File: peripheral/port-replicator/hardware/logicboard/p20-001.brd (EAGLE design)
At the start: 72 x 72 mm, 25 parts, among them IC1 74ALS04N, J0 DC9V, J11 AUDIO_JACK_3.5MM_PTH, J12 AUDIO_JACK_3.5MM_PTH, J13 AUDIO_JACK_3.5MM_PTH, J14 AUDIO_JACK_3.5MM_PTH, J21 DIN5, J22 DIN5, J23 DIN5, X0 MKDSN1,5/2-5,08

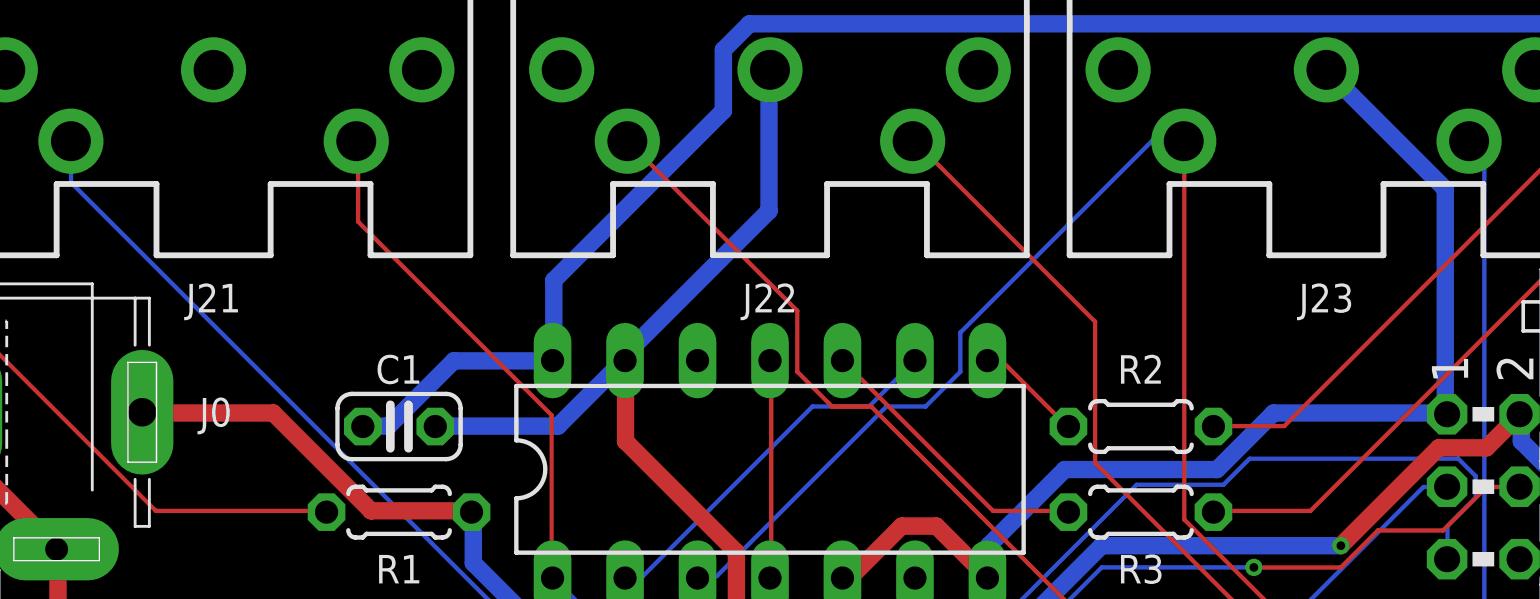
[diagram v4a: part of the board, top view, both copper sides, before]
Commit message: Renumbered parts of Port Replicator.
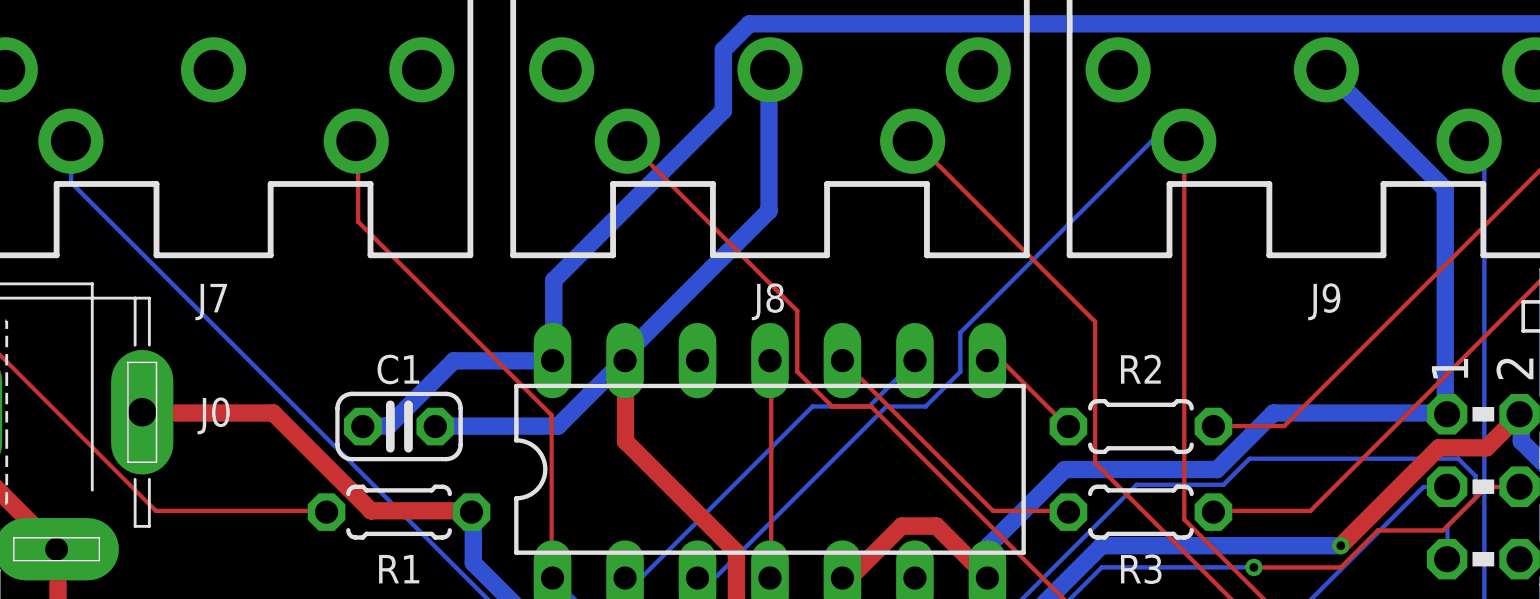
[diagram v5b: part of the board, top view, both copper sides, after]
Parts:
- renumbered J21 to J7, J22 to J8, J23 to J9
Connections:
- net MRX+: now also SV2.7; no longer SV2.6
- net MRXDTCT: now also SV2.6; no longer SV2.7
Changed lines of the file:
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@@
 <attribute name="VALUE" x="-0.43" y="27.9746" size="1.778" layer="27" ratio="10" rot="R90"/>
 </element>
-<element name="J21" library="SparkFun-Connectors" library_urn="urn:adsk.eagle:library:513" package="DIN5-RA-PTH" package3d_urn="urn:adsk.eagle:package:38294/1" value="DIN5" x="16.5" y="72" smashed="yes" rot="R180">
+<element name="J7" library="SparkFun-Connectors" library_urn="urn:adsk.eagle:library:513" package="DIN5-RA-PTH" package3d_urn="urn:adsk.eagle:package:38294/1" value="DIN5" x="16.5" y="72" smashed="yes" rot="R180">
 <attribute name="NAME" x="16.5" y="52" size="1" layer="25" ratio="20" align="top-center"/>
 <attribute name="PROD_ID" value="CONN-09481" x="16.5" y="72" size="1.778" layer="27" rot="R180" display="off"/>
 <attribute name="VALUE" x="17.77" y="68.063" size="0.6096" layer="27" font="vector" ratio="20" rot="R180"/>
 </element>
-<element name="J22" library="SparkFun-Connectors" library_urn="urn:adsk.eagle:library:513" package="DIN5-RA-PTH" package3d_urn="urn:adsk.eagle:package:38294/1" value="DIN5" x="36" y="72" smashed="yes" rot="R180">
+<element name="J8" library="SparkFun-Connectors" library_urn="urn:adsk.eagle:library:513" package="DIN5-RA-PTH" package3d_urn="urn:adsk.eagle:package:38294/1" value="DIN5" x="36" y="72" smashed="yes" rot="R180">
 <attribute name="NAME" x="36" y="52" size="1" layer="25" ratio="20" align="top-center"/>
 <attribute name="PROD_ID" value="CONN-09481" x="36" y="72" size="1.778" layer="27" rot="R180" display="off"/>
 <attribute name="VALUE" x="37.27" y="68.063" size="0.6096" layer="27" font="vector" ratio="20" rot="R180"/>
 </element>
-<element name="J23" library="SparkFun-Connectors" library_urn="urn:adsk.eagle:library:513" package="DIN5-RA-PTH" package3d_urn="urn:adsk.eagle:package:38294/1" value="DIN5" x="55.5" y="72" smashed="yes" rot="R180">
+<element name="J9" library="SparkFun-Connectors" library_urn="urn:adsk.eagle:library:513" package="DIN5-RA-PTH" package3d_urn="urn:adsk.eagle:package:38294/1" value="DIN5" x="55.5" y="72" smashed="yes" rot="R180">
 <attribute name="NAME" x="55.5" y="52" size="1" layer="25" ratio="20" align="top-center"/>
 <attribute name="PROD_ID" value="CONN-09481" x="55.5" y="72" size="1.778" layer="27" rot="R180" display="off"/>
@@
 <contactref element="J0" pad="1"/>
 <contactref element="J0" pad="2"/>
-<contactref element="J22" pad="2"/>
-<contactref element="J23" pad="2"/>
+<contactref element="J8" pad="2"/>
+<contactref element="J9" pad="2"/>
 <contactref element="J11" pad="SLEEVE"/>
 <contactref element="J12" pad="SLEEVE"/>
@@
 <wire x1="39.7764" y1="21.336" x2="39.81" y2="21.27" width="0.1524" layer="1"/>
 </signal>
-<signal name="MRX+">
-<contactref element="SV2" pad="6"/>
-</signal>
 <signal name="MRX-">
 <contactref element="SV2" pad="8"/>
 </signal>
 <signal name="MRXDTCT">
-<contactref element="SV2" pad="7"/>
+<contactref element="SV2" pad="6"/>
 </signal>
 <signal name="VCC/2" class="2">
@@
 </signal>
 <signal name="MISND">
-<contactref element="J21" pad="4"/>
+<contactref element="J7" pad="4"/>
 <contactref element="SV2" pad="4"/>
 <wire x1="61.1124" y1="44.8818" x2="62.2554" y2="44.8818" width="0.1524" layer="1"/>
@@
 </signal>
 <signal name="MIRTN">
-<contactref element="J21" pad="5"/>
+<contactref element="J7" pad="5"/>
 <contactref element="IC1" pad="1"/>
 <contactref element="SV2" pad="5"/>
@@
 </signal>
 <signal name="MORTN">
-<contactref element="J23" pad="5"/>
+<contactref element="J9" pad="5"/>
 <contactref element="SV2" pad="15"/>
 <wire x1="59.7408" y1="30.861" x2="59.7408" y2="29.718" width="0.1524" layer="16"/>
@@
 </signal>
 <signal name="MOSND">
-<contactref element="J23" pad="4"/>
+<contactref element="J9" pad="4"/>
 <contactref element="IC1" pad="3"/>
 <contactref element="SV2" pad="14"/>
@@
 <signal name="MTSND">
 <contactref element="SV2" pad="17"/>
-<contactref element="J22" pad="4"/>
+<contactref element="J8" pad="4"/>
 <wire x1="59.6646" y1="27.5844" x2="59.6646" y2="27.1272" width="0.1524" layer="1"/>
 <wire x1="39.5478" y1="47.7012" x2="59.6646" y2="27.5844" width="0.1524" layer="1"/>
@@
 <signal name="MTRTN">
 <contactref element="SV2" pad="18"/>
-<contactref element="J22" pad="5"/>
+<contactref element="J8" pad="5"/>
 <wire x1="62.2554" y1="28.2702" x2="62.2554" y2="27.1272" width="0.1524" layer="1"/>
 <wire x1="60.7314" y1="29.7942" x2="62.2554" y2="28.2702" width="0.1524" layer="1"/>
@@
 <wire x1="38.5572" y1="49.3014" x2="38.54" y2="49.31" width="0.1524" layer="1"/>
 </signal>
+<signal name="MRX+">
+<contactref element="SV2" pad="7"/>
+</signal>
 </signals>

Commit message: Redesign of port rep.
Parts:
- removed JP1: (no value), adafruit:2X04
- added RN1, RN2: (no value), resistor-net:RN-5
- added S2: (no value), switch-dil:DIP04S
- moved S1 2.00 mm to (36.0, 29.5)
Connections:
- new net N$5: RN2.2, S2.8
- new net N$6: RN2.3, S2.7
- new net N$7: RN2.4, S2.6
- new net N$8: RN2.5, S2.5
- net DTCT1: now also J11.TSH, RN1.2, S2.1; no longer JP1.2
- net DTCT2: now also J12.TSH, RN1.3, S2.2; no longer JP1.4
- net DTCT3: now also J13.TSH, RN1.4, S2.3; no longer JP1.6
- net DTCT4: now also J14.TSH, RN1.5, S2.4; no longer JP1.8
- net GND: now also RN1.1; no longer JP1.1, JP1.3, JP1.5, JP1.7
- net VCC/2: now also RN2.1
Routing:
- net DTCT4: track 34.0 -> 88.3 mm
- net DTCT3: track 29.4 -> 60.4 mm
- net GND: track 293.5 -> 267.9 mm
- net N$5: track 0.00 -> 18.8 mm
- net N$6: track 0.00 -> 17.3 mm
- net DTCT1: track 20.1 -> 36.9 mm
- net VCC/2: track 79.2 -> 96.0 mm
- net N$7: track 0.00 -> 14.5 mm
- net MOSND: track 54.8 -> 67.9 mm
- net N$8: track 0.00 -> 13.1 mm
- net V+: track 90.2 -> 102.5 mm, vias 1 -> 0
- net ANLG2R: track 21.4 -> 32.5 mm
- net LED0: track 117.8 -> 125.8 mm
- net DTCT2: track 24.7 -> 32.6 mm
- net MISND: track 61.5 -> 67.6 mm, vias 1 -> 0
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- removed copper zone on layer 1, net GND
- removed copper zone on layer 16, net GND
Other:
- board text added: "Active"
- board text added: "Passive"

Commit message: Renumbered parts of Pineapple II and port rep.
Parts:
- renumbered C1 to C11, IC1 to IC11, R1 to R11
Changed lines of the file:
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@@
 </element>
 <element name="U$1" library="pineapple" package="PINEAPPLE450_SILK" value="PINEAPPLE450_SILK" x="36" y="33.5" smashed="yes" rot="MR0"/>
-<element name="C1" library="resistor" library_urn="urn:adsk.eagle:library:348" package="C025-024X044" package3d_urn="urn:adsk.eagle:package:23630/1" value="10n" x="23" y="47" smashed="yes">
+<element name="C11" library="resistor" library_urn="urn:adsk.eagle:library:348" package="C025-024X044" package3d_urn="urn:adsk.eagle:package:23630/1" value="10n" x="23" y="47" smashed="yes">
 <attribute name="NAME" x="23" y="48.5" size="1" layer="25" ratio="10" align="bottom-center"/>
 <attribute name="VALUE" x="23" y="45" size="0.8128" layer="27" ratio="10" align="bottom-center"/>
@@
 <attribute name="VALUE" x="59.667" y="5.23" size="0.6096" layer="27" font="vector" ratio="20" rot="R90"/>
 </element>
-<element name="IC1" library="74xx-us" library_urn="urn:adsk.eagle:library:88" package="DIL14" package3d_urn="urn:adsk.eagle:package:16407/2" value="74ALS04N" x="36" y="45.5" smashed="yes">
+<element name="IC11" library="74xx-us" library_urn="urn:adsk.eagle:library:88" package="DIL14" package3d_urn="urn:adsk.eagle:package:16407/2" value="74ALS04N" x="36" y="45.5" smashed="yes">
 <attribute name="NAME" x="36" y="40" size="1" layer="25" ratio="10" align="top-center"/>
 <attribute name="POPULARITY" value="10" x="36" y="45.5" size="1.778" layer="27" display="off"/>
 <attribute name="VALUE" x="29.269" y="44.865" size="1.27" layer="27" ratio="10"/>
 </element>
-<element name="R1" library="rcl" library_urn="urn:adsk.eagle:library:334" package="0204/5" package3d_urn="urn:adsk.eagle:package:23488/1" value="" x="23" y="44" smashed="yes">
+<element name="R11" library="rcl" library_urn="urn:adsk.eagle:library:334" package="0204/5" package3d_urn="urn:adsk.eagle:package:23488/1" value="" x="23" y="44" smashed="yes">
 <attribute name="NAME" x="23" y="42.5" size="1" layer="25" ratio="10" align="top-center"/>
 <attribute name="POPULARITY" value="35" x="23" y="44" size="1.778" layer="27" display="off"/>
@@
 <signals>
 <signal name="GND" class="1">
-<contactref element="C1" pad="2"/>
+<contactref element="C11" pad="2"/>
 <contactref element="SV1" pad="1"/>
 <contactref element="SV1" pad="5"/>
@@
 <contactref element="J13" pad="SLEEVE"/>
 <contactref element="J14" pad="SLEEVE"/>
-<contactref element="IC1" pad="13"/>
-<contactref element="IC1" pad="5"/>
+<contactref element="IC11" pad="13"/>
+<contactref element="IC11" pad="5"/>
 <contactref element="LED4" pad="K"/>
-<contactref element="IC1" pad="7"/>
+<contactref element="IC11" pad="7"/>
 <contactref element="X0" pad="1"/>
 <contactref element="S1" pad="1"/>
@@
 </signal>
 <signal name="VCC" class="2">
-<contactref element="C1" pad="1"/>
+<contactref element="C11" pad="1"/>
 <contactref element="LED2" pad="A"/>
 <contactref element="LED3" pad="A"/>
-<contactref element="IC1" pad="14"/>
+<contactref element="IC11" pad="14"/>
 <contactref element="SV2" pad="12"/>
 <wire x1="22.6314" y1="47.0154" x2="21.7932" y2="47.0154" width="0.6096" layer="16"/>
@@
 <signal name="MIRTN">
 <contactref element="J7" pad="5"/>
-<contactref element="IC1" pad="1"/>
+<contactref element="IC11" pad="1"/>
 <contactref element="SV2" pad="5"/>
 <wire x1="28.3464" y1="47.3964" x2="28.3464" y2="41.7576" width="0.1524" layer="1"/>
@@
 <signal name="MOSND">
 <contactref element="J9" pad="4"/>
-<contactref element="IC1" pad="3"/>
+<contactref element="IC11" pad="3"/>
 <contactref element="SV2" pad="14"/>
 <wire x1="33.528" y1="47.3964" x2="33.528" y2="41.7576" width="0.1524" layer="1"/>
@@
 <contactref element="SV2" pad="2"/>
 <contactref element="J0" pad="3"/>
-<contactref element="R1" pad="2"/>
+<contactref element="R11" pad="2"/>
 <contactref element="X0" pad="2"/>
 <wire x1="22.0218" y1="44.0436" x2="25.527" y2="44.0436" width="0.6096" layer="16"/>
@@
 </signal>
 <signal name="LEDPWR">
-<contactref element="R1" pad="1"/>
+<contactref element="R11" pad="1"/>
 <contactref element="LED4" pad="A"/>
 <wire x1="14.478" y1="44.0436" x2="20.4216" y2="44.0436" width="0.1524" layer="1"/>
@@
 </signal>
 <signal name="N$1">
-<contactref element="IC1" pad="2"/>
-<contactref element="IC1" pad="9"/>
+<contactref element="IC11" pad="2"/>
+<contactref element="IC11" pad="9"/>
 <wire x1="31.5468" y1="41.7576" x2="30.9372" y2="41.7576" width="0.1524" layer="16"/>
 <wire x1="37.4904" y1="47.7012" x2="31.5468" y2="41.7576" width="0.1524" layer="16"/>
@@
 </signal>
 <signal name="N$2">
-<contactref element="IC1" pad="4"/>
-<contactref element="IC1" pad="11"/>
+<contactref element="IC11" pad="4"/>
+<contactref element="IC11" pad="11"/>
 <wire x1="36.0426" y1="49.3014" x2="36.0426" y2="41.7576" width="0.1524" layer="1"/>
 <wire x1="36.0426" y1="41.7576" x2="36" y2="41.69" width="0.1524" layer="1"/>
@@
 </signal>
 <signal name="N$3">
-<contactref element="IC1" pad="8"/>
+<contactref element="IC11" pad="8"/>
 <contactref element="R2" pad="1"/>
 <wire x1="44.1198" y1="49.3014" x2="43.6626" y2="49.3014" width="0.1524" layer="1"/>
@@
 </signal>
 <signal name="N$4">
-<contactref element="IC1" pad="10"/>
+<contactref element="IC11" pad="10"/>
 <contactref element="R3" pad="1"/>
 <wire x1="43.815" y1="44.0436" x2="46.4058" y2="44.0436" width="0.1524" layer="1"/>
